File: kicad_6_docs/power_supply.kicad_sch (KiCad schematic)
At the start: 53 parts, among them J3 iec_power_entry, T1 power_transformer, U1 TL072, U10 TL072, U11 TL072, U12 TL072, U13 TL072, U14 LM317_TO-220, U15 LM337_TO220, U2 SSI2164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

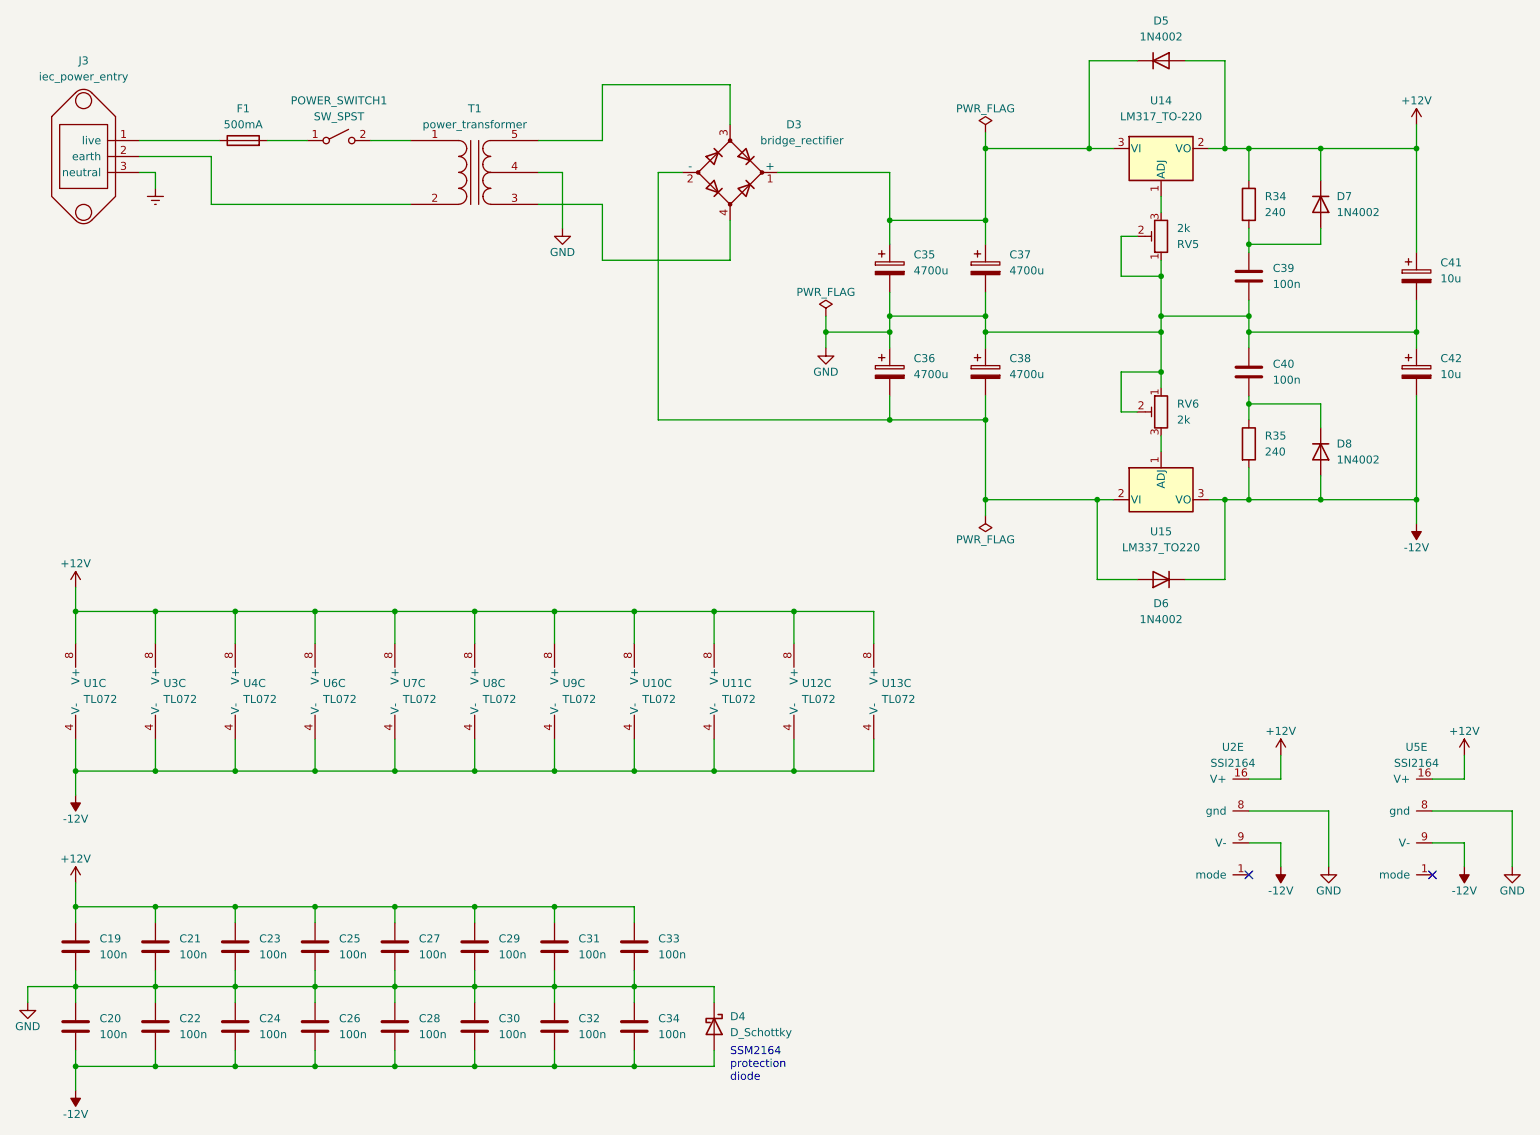
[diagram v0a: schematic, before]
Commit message: Fix power supply errors, tidy up schematic
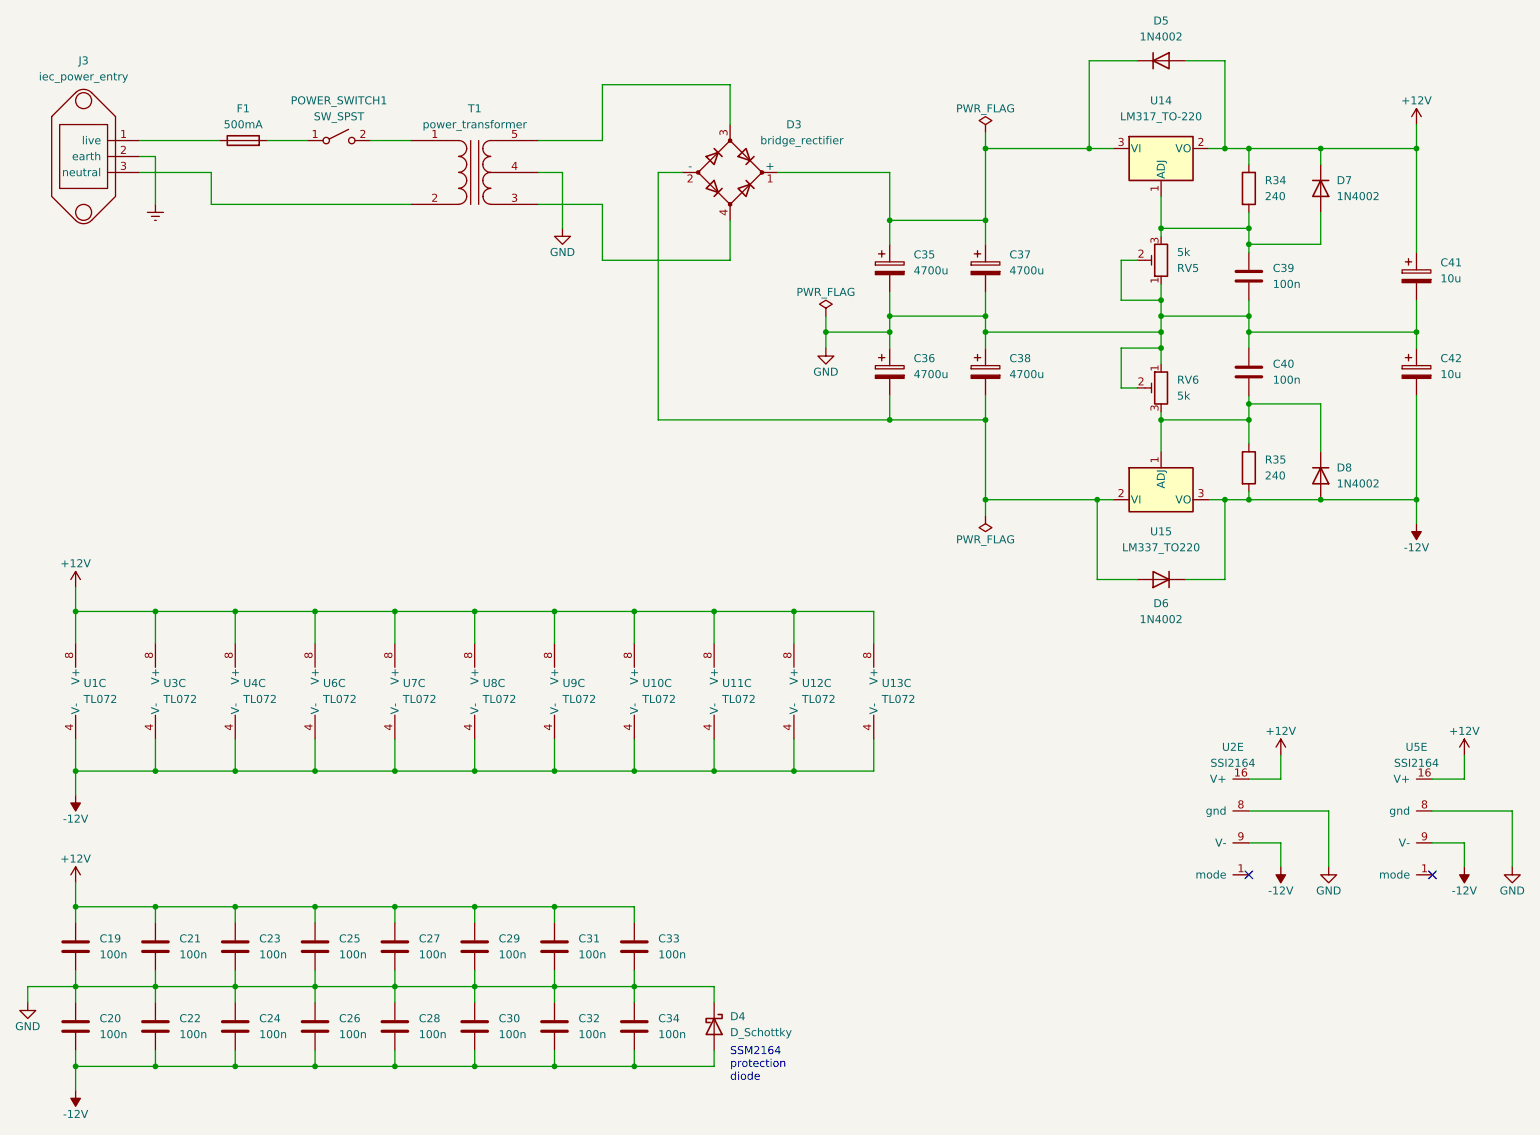
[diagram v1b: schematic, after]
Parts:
- RV5, RV6: value 2k -> 5k
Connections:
- net Earth: now also J3.2 (earth); no longer J3.3 (neutral)
- net at C39.1, D7.2 (A), R34.2: now also RV5.3, U14.1 (ADJ)
- net at C40.2, D8.1 (K), R35.1: now also RV6.3, U15.1 (ADJ)
- net at T1.2 (AB): now also J3.3 (neutral); no longer J3.2 (earth)
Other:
- moved on the sheet: D7, D8, R34, R35, RV5, RV6
